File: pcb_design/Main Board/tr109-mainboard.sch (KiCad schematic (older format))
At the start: 23 parts, among them J1 Raspberry Pi Zero W, J2 ST7735_Screen, J3 Conn_01x04_Female, J4 Conn_01x09_Female, J5 Conn_01x03_Female, J6 Conn_01x02_Female-Connector, J7 Conn_01x03_Female, Q1 2N2222A, U1 CAP1208, U2 74HC595

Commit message: cleanup and revisions
changes to the sensor and main boards
clean up of the blender file to remove some deprecated meshes
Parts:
- removed C2: 10uF, Capacitor_SMD:C_0603_1608Metric_Pad1.05x0.95mm_HandSolder, symbol Device:CP
- removed Q1: 2N2222A, footprints:SSTA06HZGT116, symbol dk_Transistors-Bipolar-BJT-Single:2N2222A
- removed R3: 15k, Resistor_SMD:R_0603_1608Metric_Pad1.05x0.95mm_HandSolder, symbol Device:R
- removed R4: 8, Resistor_SMD:R_0603_1608Metric_Pad1.05x0.95mm_HandSolder, symbol Device:R
- added C2: 1uF, Capacitor_SMD:C_0603_1608Metric_Pad1.05x0.95mm_HandSolder, symbol Device:C
- added C3: 10uF, Capacitor_SMD:C_0603_1608Metric_Pad1.05x0.95mm_HandSolder, symbol Device:C
- added RV1: 10K, Potentiometer_SMD:Potentiometer_Bourns_3214W_Vertical, symbol Device:R_POT
- added U3: PAM8302AAS, Main Board:SOIC-8, symbol Amplifier_Audio:PAM8302AAS
- C1: value 100nF -> 1uF
- J6: symbol oshpark-2layer-rescue:Conn_01x02_Female-Connector -> Connector:Conn_01x02_Female
- R1: value 270 -> 100
- R2: value 150 -> 100
- U1: symbol Sensor_Touch:CAP1208 -> tr109-mainboard-rescue:CAP1208-Sensor_Touch
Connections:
- wire segments 24 -> 35
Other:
- moved on the sheet: J6
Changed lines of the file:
@@
 LED4
 $Comp
-L Sensor_Touch:CAP1208 U1
+L tr109-mainboard-rescue:CAP1208-Sensor_Touch U1
 U 1 1 5F245663
 P 4100 5800
@@
 Text GLabel 2450 1250 1    50   Input ~ 0
 5V
-Text GLabel 1750 2050 0    50   Input ~ 0
+Text GLabel 1750 2150 0    50   Input ~ 0
 Hall_Effect_Sensor
 Text GLabel 3500 5450 0    50   Input ~ 0
@@
 Hall_Effect_Sensor
 $Comp
-L dk_Transistors-Bipolar-BJT-Single:2N2222A Q1
-U 1 1 5FC250B2
-P 6400 1450
-F 0 "Q1" H 6588 1503 60  0000 L CNN
-F 1 "2N2222A" H 6588 1397 60  0000 L CNN
-F 2 "footprints:SSTA06HZGT116" H 6600 1650 60  0001 L CNN
-F 3 "https://my.centralsemi.com/get_document.php?cmp=1&mergetype=pd&mergepath=pd&pdf_id=2N2221A.PDF" H 6600 1750 60  0001 L CNN
-F 4 "2N2222ACS-ND" H 6600 1850 60  0001 L CNN "Digi-Key_PN"
-F 5 "2N2222A" H 6600 1950 60  0001 L CNN "MPN"
-F 6 "Discrete Semiconductor Products" H 6600 2050 60  0001 L CNN "Category"
-F 7 "Transistors - Bipolar (BJT) - Single" H 6600 2150 60  0001 L CNN "Family"
-F 8 "https://my.centralsemi.com/get_document.php?cmp=1&mergetype=pd&mergepath=pd&pdf_id=2N2221A.PDF" H 6600 2250 60  0001 L CNN "DK_Datasheet_Link"
-F 9 "/product-detail/en/central-semiconductor-corp/2N2222A/2N2222ACS-ND/4806845" H 6600 2350 60  0001 L CNN "DK_Detail_Page"
-F 10 "TRANS NPN 40V 0.8A TO-18" H 6600 2450 60  0001 L CNN "Description"
-F 11 "Central Semiconductor Corp" H 6600 2550 60  0001 L CNN "Manufacturer"
-F 12 "Active" H 6600 2650 60  0001 L CNN "Status"
-	1    6400 1450
-	1    0    0    -1
-$EndComp
-$Comp
-L Device:R R4
-U 1 1 5FC269BF
-P 6650 1100
-F 0 "R4" V 6443 1100 50  0000 C CNN
-F 1 "8" V 6534 1100 50  0000 C CNN
-F 2 "Resistor_SMD:R_0603_1608Metric_Pad1.05x0.95mm_HandSolder" V 6580 1100 50  0001 C CNN
-F 3 "~" H 6650 1100 50  0001 C CNN
-	1    6650 1100
-	0    1    1    0
-$EndComp
-$Comp
-L Device:R R3
-U 1 1 5FC2856A
-P 6200 1150
-F 0 "R3" H 6130 1104 50  0000 R CNN
-F 1 "15k" H 6130 1195 50  0000 R CNN
-F 2 "Resistor_SMD:R_0603_1608Metric_Pad1.05x0.95mm_HandSolder" V 6130 1150 50  0001 C CNN
-F 3 "~" H 6200 1150 50  0001 C CNN
-	1    6200 1150
-	-1   0    0    1
-$EndComp
-$Comp
-L oshpark-2layer-rescue:Conn_01x02_Female-Connector J6
+L Connector:Conn_01x02_Female J6
 U 1 1 5FC2A999
-P 7200 850
-F 0 "J6" H 7228 826 50  0000 L CNN
-F 1 "Conn_01x02_Female-Connector" H 7228 735 50  0000 L CNN
-F 2 "Connector_PinHeader_2.54mm:PinHeader_1x02_P2.54mm_Vertical" H 7200 850 50  0001 C CNN
-F 3 "" H 7200 850 50  0001 C CNN
-	1    7200 850
-	1    0    0    -1
-$EndComp
-Wire Wire Line
-	6500 1100 6500 1250
-Wire Wire Line
-	6800 1100 7000 1100
-Wire Wire Line
-	7000 1100 7000 950
-Wire Wire Line
-	7000 850  6200 850
-Wire Wire Line
-	6200 850  6200 1000
-Wire Wire Line
-	6200 1300 6200 1450
-$Comp
-L Device:C C1
-U 1 1 5FC2DDBE
-P 5800 1600
-F 0 "C1" H 5915 1646 50  0000 L CNN
-F 1 "100nF" H 5915 1555 50  0000 L CNN
-F 2 "Capacitor_SMD:C_0603_1608Metric_Pad1.05x0.95mm_HandSolder" H 5838 1450 50  0001 C CNN
-F 3 "~" H 5800 1600 50  0001 C CNN
-	1    5800 1600
-	1    0    0    -1
-$EndComp
-$Comp
-L Device:CP C2
-U 1 1 5FC2F329
-P 6000 1450
-F 0 "C2" V 6255 1450 50  0000 C CNN
-F 1 "10uF" V 6164 1450 50  0000 C CNN
-F 2 "Capacitor_SMD:C_0603_1608Metric_Pad1.05x0.95mm_HandSolder" H 6038 1300 50  0001 C CNN
-F 3 "~" H 6000 1450 50  0001 C CNN
-	1    6000 1450
-	0    -1   -1   0
-$EndComp
-Wire Wire Line
-	6200 1450 6150 1450
-Connection ~ 6200 1450
-Wire Wire Line
-	5850 1450 5800 1450
-Wire Wire Line
-	6500 1750 6500 1650
-$Comp
-L Device:R R2
-U 1 1 5FC313ED
-P 5450 1600
-F 0 "R2" H 5380 1554 50  0000 R CNN
-F 1 "150" H 5380 1645 50  0000 R CNN
-F 2 "Resistor_SMD:R_0603_1608Metric_Pad1.05x0.95mm_HandSolder" V 5380 1600 50  0001 C CNN
-F 3 "~" H 5450 1600 50  0001 C CNN
-	1    5450 1600
-	-1   0    0    1
-$EndComp
-Wire Wire Line
-	5800 1750 5450 1750
-Wire Wire Line
-	5800 1450 5450 1450
-Connection ~ 5800 1450
-$Comp
-L Device:R R1
-U 1 1 5FC32D30
-P 5200 1450
-F 0 "R1" V 5407 1450 50  0000 C CNN
-F 1 "270" V 5316 1450 50  0000 C CNN
-F 2 "Resistor_SMD:R_0603_1608Metric_Pad1.05x0.95mm_HandSolder" V 5130 1450 50  0001 C CNN
-F 3 "~" H 5200 1450 50  0001 C CNN
-	1    5200 1450
-	0    -1   -1   0
-$EndComp
-Wire Wire Line
-	5450 1450 5350 1450
-Connection ~ 5450 1450
+P 6700 1500
+F 0 "J6" H 6728 1476 50  0000 L CNN
+F 1 "Conn_01x02_Female-Connector" H 6728 1385 50  0000 L CNN
+F 2 "Connector_PinHeader_2.54mm:PinHeader_1x02_P2.54mm_Vertical" H 6700 1500 50  0001 C CNN
+F 3 "" H 6700 1500 50  0001 C CNN
+	1    6700 1500
+	1    0    0    -1
+$EndComp
 Text GLabel 3350 3350 2    50   Input ~ 0
 AUDIO
-Text GLabel 5050 1450 0    50   Input ~ 0
-AUDIO
-Text GLabel 6200 850  1    50   Input ~ 0
-5V
-Text GLabel 5450 1750 3    50   Input ~ 0
-GND
-Text GLabel 4700 1900 0    50   Input ~ 0
-Bat_GPIO
 Text GLabel 3350 2350 2    50   Input ~ 0
 Bat_GPIO
@@
 Text GLabel 1750 3150 0    50   Input ~ 0
 Hall_Effect_Sensor2
-Text GLabel 6500 1750 3    50   Input ~ 0
-GND
 Text GLabel 3500 6050 0    50   Input ~ 0
 Cap_7
 Text GLabel 4700 6050 2    50   Input ~ 0
 Cap_7
+$Comp
+L Amplifier_Audio:PAM8302AAS U3
+U 1 1 60ABCA11
+P 5850 1700
+F 0 "U3" H 6100 2600 50  0000 C CNN
+F 1 "PAM8302AAS" H 6100 2500 50  0000 C CNN
+F 2 "Main Board:SOIC-8" H 5850 1700 50  0001 C CNN
+F 3 "https://www.diodes.com/assets/Datasheets/PAM8302A.pdf" H 5850 1700 50  0001 C CNN
+	1    5850 1700
+	1    0    0    -1
+$EndComp
+$Comp
+L Device:R_POT RV1
+U 1 1 60ABDB90
+P 4700 1200
+F 0 "RV1" H 4631 1246 50  0000 R CNN
+F 1 "10K" H 4631 1155 50  0000 R CNN
+F 2 "Potentiometer_SMD:Potentiometer_Bourns_3214W_Vertical" H 4700 1200 50  0001 C CNN
+F 3 "~" H 4700 1200 50  0001 C CNN
+	1    4700 1200
+	1    0    0    -1
+$EndComp
+$Comp
+L Device:C C1
+U 1 1 60ABF3BD
+P 5000 1200
+F 0 "C1" V 4748 1200 50  0000 C CNN
+F 1 "1uF" V 4839 1200 50  0000 C CNN
+F 2 "Capacitor_SMD:C_0603_1608Metric_Pad1.05x0.95mm_HandSolder" H 5038 1050 50  0001 C CNN
+F 3 "~" H 5000 1200 50  0001 C CNN
+	1    5000 1200
+	0    1    1    0
+$EndComp
+$Comp
+L Device:R R1
+U 1 1 60ABFD3B
+P 5300 1200
+F 0 "R1" V 5093 1200 50  0000 C CNN
+F 1 "100" V 5184 1200 50  0000 C CNN
+F 2 "Resistor_SMD:R_0603_1608Metric_Pad1.05x0.95mm_HandSolder" V 5230 1200 50  0001 C CNN
+F 3 "~" H 5300 1200 50  0001 C CNN
+	1    5300 1200
+	0    1    1    0
+$EndComp
+$Comp
+L Device:R R2
+U 1 1 60AC08CB
+P 5300 1700
+F 0 "R2" V 5093 1700 50  0000 C CNN
+F 1 "100" V 5184 1700 50  0000 C CNN
+F 2 "Resistor_SMD:R_0603_1608Metric_Pad1.05x0.95mm_HandSolder" V 5230 1700 50  0001 C CNN
+F 3 "~" H 5300 1700 50  0001 C CNN
+	1    5300 1700
+	0    1    1    0
+$EndComp
+$Comp
+L Device:C C2
+U 1 1 60AC1063
+P 5000 1700
+F 0 "C2" V 4748 1700 50  0000 C CNN
+F 1 "1uF" V 4839 1700 50  0000 C CNN
+F 2 "Capacitor_SMD:C_0603_1608Metric_Pad1.05x0.95mm_HandSolder" H 5038 1550 50  0001 C CNN
+F 3 "~" H 5000 1700 50  0001 C CNN
+	1    5000 1700
+	0    1    1    0
+$EndComp
+Wire Wire Line
+	5450 1200 5450 1500
+Text GLabel 4850 2000 3    50   Input ~ 0
+GND
+Wire Wire Line
+	4700 1350 4850 1350
+Wire Wire Line
+	4850 1350 4850 1700
+Wire Wire Line
+	4850 1700 4850 2000
+Connection ~ 4850 1700
+Text GLabel 4250 900  0    50   Input ~ 0
+AUDIO
+Text GLabel 5150 2050 0    50   Input ~ 0
+5V
+Text GLabel 5250 2350 3    50   Input ~ 0
+GND
+Text GLabel 5850 2100 3    50   Input ~ 0
+GND
+$Comp
+L Device:C C3
+U 1 1 60AC6DC2
+P 5250 2200
+F 0 "C3" H 5135 2154 50  0000 R CNN
+F 1 "10uF" H 5135 2245 50  0000 R CNN
+F 2 "Capacitor_SMD:C_0603_1608Metric_Pad1.05x0.95mm_HandSolder" H 5288 2050 50  0001 C CNN
+F 3 "~" H 5250 2200 50  0001 C CNN
+	1    5250 2200
+	-1   0    0    1
+$EndComp
+Connection ~ 5250 2050
+Wire Wire Line
+	5250 2050 5150 2050
+Wire Wire Line
+	5850 1350 5850 1300
+Wire Wire Line
+	5850 1150 6350 1150
+Wire Wire Line
+	6350 1150 6350 2450
+Wire Wire Line
+	6350 2450 5600 2450
+Wire Wire Line
+	5600 2450 5600 2050
+Connection ~ 5850 1300
+Wire Wire Line
+	5850 1300 5850 1150
+Wire Wire Line
+	5250 2050 5450 2050
+Wire Wire Line
+	5450 1900 5450 2050
+Connection ~ 5450 2050
+Wire Wire Line
+	5450 2050 5600 2050
+Wire Wire Line
+	6250 1500 6500 1500
+Wire Wire Line
+	6250 1700 6500 1700
+Wire Wire Line
+	6500 1700 6500 1600
+Wire Wire Line
+	4250 900  4700 900
+Wire Wire Line
+	4700 900  4700 1050
+Wire Wire Line
+	4150 5750 4150 5800
+Wire Wire Line
+	4000 5800 4050 5800
+Wire Wire Line
+	4050 5800 4050 5750
+Wire Wire Line
+	6750 1400 6750 1350
+Entry Wire Line
+	9350 6400 9450 6500
 $EndSCHEMATC

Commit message: Pcb and shell design work
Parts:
- J4: value Conn_01x09_Female -> Conn_01x11_Female; footprint Connector_PinHeader_2.54mm:PinHeader_1x09_P2.54mm_Vertical -> Connector_PinHeader_2.54mm:PinHeader_1x11_P2.54mm_Vertical; symbol Connector:Conn_01x09_Female -> Connector:Conn_01x11_Female
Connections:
- net labels added: Cap_8, Shift_Clock_Sensor_Board, Shift_Latch_Sensor_Board, Shift_Serial_Sensor_Board
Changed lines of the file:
@@
 Text GLabel 2450 1250 1    50   Input ~ 0
 5V
-Text GLabel 1750 2150 0    50   Input ~ 0
+Text GLabel 3350 3250 2    50   Input ~ 0
 Hall_Effect_Sensor
 Text GLabel 3500 5450 0    50   Input ~ 0
@@
 Text GLabel 8400 2650 0    50   Input ~ 0
 LED5
-Text GLabel 9200 4000 0    50   Input ~ 0
+Text GLabel 9200 3900 0    50   Input ~ 0
 Cap_6
-Text GLabel 9200 3900 0    50   Input ~ 0
+Text GLabel 9200 3800 0    50   Input ~ 0
 Cap_5
-Text GLabel 9200 3800 0    50   Input ~ 0
+Text GLabel 9200 3700 0    50   Input ~ 0
 Cap_4
-Text GLabel 9200 3700 0    50   Input ~ 0
+Text GLabel 9200 3600 0    50   Input ~ 0
 Cap_3
-Text GLabel 9200 3600 0    50   Input ~ 0
+Text GLabel 9200 3500 0    50   Input ~ 0
 Cap_2
-Text GLabel 9200 3500 0    50   Input ~ 0
+Text GLabel 9200 3400 0    50   Input ~ 0
 Cap_1
-Text GLabel 9200 3400 0    50   Input ~ 0
+Text GLabel 9200 3300 0    50   Input ~ 0
 Bat_GPIO
+Text GLabel 9200 3100 0    50   Input ~ 0
+GND
 Text GLabel 9200 3200 0    50   Input ~ 0
-GND
-Text GLabel 9200 3300 0    50   Input ~ 0
 5V
 $Comp
@@
 GND
 $Comp
-L Connector:Conn_01x09_Female J4
+L Connector:Conn_01x11_Female J4
 U 1 1 5F576896
 P 9400 3600
 F 0 "J4" H 9428 3626 50  0000 L CNN
-F 1 "Conn_01x09_Female" H 9428 3535 50  0000 L CNN
-F 2 "Connector_PinHeader_2.54mm:PinHeader_1x09_P2.54mm_Vertical" H 9400 3600 50  0001 C CNN
+F 1 "Conn_01x11_Female" H 9428 3535 50  0000 L CNN
+F 2 "Connector_PinHeader_2.54mm:PinHeader_1x11_P2.54mm_Vertical" H 9400 3600 50  0001 C CNN
 F 3 "~" H 9400 3600 50  0001 C CNN
 	1    9400 3600
@@
 Text GLabel 9250 1450 0    50   Input ~ 0
 Hall_Effect_Sensor2
-Text GLabel 1750 3150 0    50   Input ~ 0
+Text GLabel 3350 2250 2    50   Input ~ 0
 Hall_Effect_Sensor2
 Text GLabel 3500 6050 0    50   Input ~ 0
 Cap_7
 Text GLabel 4700 6050 2    50   Input ~ 0
-Cap_7
+Cap_8
 $Comp
 L Amplifier_Audio:PAM8302AAS U3
@@
 Wire Wire Line
 	6750 1400 6750 1350
-Entry Wire Line
-	9350 6400 9450 6500
+Text GLabel 1750 2350 0    50   Input ~ 0
+Shift_Serial_Sensor_Board
+Text GLabel 1750 2550 0    50   Input ~ 0
+Shift_Latch_Sensor_Board
+Text GLabel 1750 3150 0    50   Input ~ 0
+Shift_Clock_Sensor_Board
+Text GLabel 9200 4000 0    50   Input ~ 0
+Cap_7
+Text GLabel 9200 4100 0    50   Input ~ 0
+Cap_8
 $EndSCHEMATC

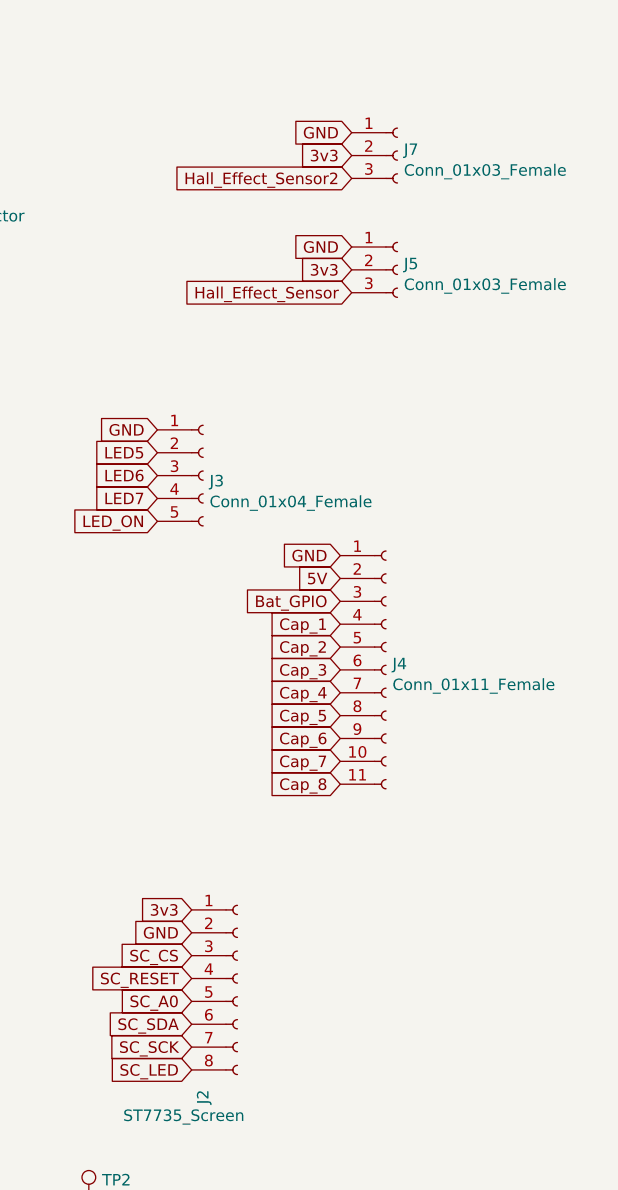
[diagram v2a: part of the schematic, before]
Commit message: Rev 3 board changes, blender file changes
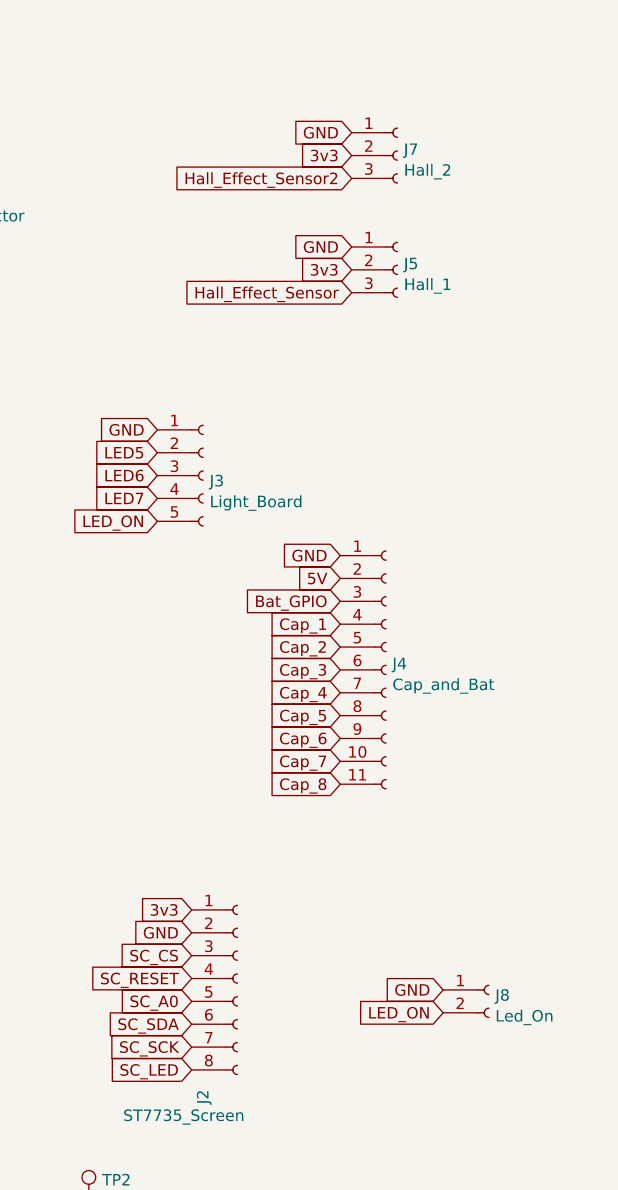
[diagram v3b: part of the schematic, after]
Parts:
- added J8: Led_On, Connector_PinHeader_2.54mm:PinHeader_1x02_P2.54mm_Vertical, symbol Connector:Conn_01x02_Female
- J3: value Conn_01x04_Female -> Light_Board
- J4: value Conn_01x11_Female -> Cap_and_Bat
- J5: value Conn_01x03_Female -> Hall_1
- J7: value Conn_01x03_Female -> Hall_2
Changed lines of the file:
@@
 P 8600 2750
 F 0 "J3" H 8628 2726 50  0000 L CNN
-F 1 "Conn_01x04_Female" H 8628 2635 50  0000 L CNN
+F 1 "Light_Board" H 8628 2635 50  0000 L CNN
 F 2 "Connector_PinHeader_2.54mm:PinHeader_1x05_P2.54mm_Vertical" H 8600 2750 50  0001 C CNN
 F 3 "~" H 8600 2750 50  0001 C CNN
@@
 P 9400 3600
 F 0 "J4" H 9428 3626 50  0000 L CNN
-F 1 "Conn_01x11_Female" H 9428 3535 50  0000 L CNN
+F 1 "Cap_and_Bat" H 9428 3535 50  0000 L CNN
 F 2 "Connector_PinHeader_2.54mm:PinHeader_1x11_P2.54mm_Vertical" H 9400 3600 50  0001 C CNN
 F 3 "~" H 9400 3600 50  0001 C CNN
@@
 P 9450 1850
 F 0 "J5" H 9478 1876 50  0000 L CNN
-F 1 "Conn_01x03_Female" H 9478 1785 50  0000 L CNN
+F 1 "Hall_1" H 9478 1785 50  0000 L CNN
 F 2 "Connector_PinHeader_2.54mm:PinHeader_1x03_P2.54mm_Vertical" H 9450 1850 50  0001 C CNN
 F 3 "~" H 9450 1850 50  0001 C CNN
@@
 P 9450 1350
 F 0 "J7" H 9478 1376 50  0000 L CNN
-F 1 "Conn_01x03_Female" H 9478 1285 50  0000 L CNN
+F 1 "Hall_2" H 9478 1285 50  0000 L CNN
 F 2 "Connector_PinHeader_2.54mm:PinHeader_1x03_P2.54mm_Vertical" H 9450 1350 50  0001 C CNN
 F 3 "~" H 9450 1350 50  0001 C CNN
@@
 Text GLabel 9200 4100 0    50   Input ~ 0
 Cap_8
+$Comp
+L Connector:Conn_01x02_Female J8
+U 1 1 60C056D7
+P 9850 5000
+F 0 "J8" H 9878 4976 50  0000 L CNN
+F 1 "Led_On" H 9878 4885 50  0000 L CNN
+F 2 "Connector_PinHeader_2.54mm:PinHeader_1x02_P2.54mm_Vertical" H 9850 5000 50  0001 C CNN
+F 3 "~" H 9850 5000 50  0001 C CNN
+	1    9850 5000
+	1    0    0    -1
+$EndComp
+Text GLabel 9650 5100 0    50   Input ~ 0
+LED_ON
+Text GLabel 9650 5000 0    50   Input ~ 0
+GND
 $EndSCHEMATC

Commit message: Pcb and enclosure changes for proto 01
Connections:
- net labels added: BUT1, BUT2, BUT3
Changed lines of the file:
@@
 Text GLabel 9650 5000 0    50   Input ~ 0
 GND
+Text GLabel 1750 2050 0    50   Input ~ 0
+BUT1
+Text GLabel 1750 3250 0    50   Input ~ 0
+BUT2
+Text GLabel 1750 2750 0    50   Input ~ 0
+BUT3
 $EndSCHEMATC

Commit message: changes to shell and pcb
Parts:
- added J10: raw_audio_out, Connector_PinHeader_2.54mm:PinHeader_1x01_P2.54mm_Vertical, symbol Connector:Conn_01x01_Female
- added J9: i2c_bus, Connector_PinHeader_2.54mm:PinHeader_1x02_P2.54mm_Vertical, symbol Connector:Conn_01x02_Female
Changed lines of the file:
@@
 Text GLabel 1750 2750 0    50   Input ~ 0
 BUT3
+$Comp
+L Connector:Conn_01x02_Female J9
+U 1 1 610ACCCB
+P 9850 5600
+F 0 "J9" H 9878 5576 50  0000 L CNN
+F 1 "i2c_bus" H 9878 5485 50  0000 L CNN
+F 2 "Connector_PinHeader_2.54mm:PinHeader_1x02_P2.54mm_Vertical" H 9850 5600 50  0001 C CNN
+F 3 "~" H 9850 5600 50  0001 C CNN
+	1    9850 5600
+	1    0    0    -1
+$EndComp
+Text GLabel 9650 5700 0    50   Input ~ 0
+SDA
+Text GLabel 9650 5600 0    50   Input ~ 0
+SCL
+$Comp
+L Connector:Conn_01x01_Female J10
+U 1 1 610B2E38
+P 9850 6000
+F 0 "J10" H 9878 6026 50  0000 L CNN
+F 1 "raw_audio_out" H 9878 5935 50  0000 L CNN
+F 2 "Connector_PinHeader_2.54mm:PinHeader_1x01_P2.54mm_Vertical" H 9850 6000 50  0001 C CNN
+F 3 "~" H 9850 6000 50  0001 C CNN
+	1    9850 6000
+	1    0    0    -1
+$EndComp
+Text GLabel 9650 6000 0    50   Input ~ 0
+AUDIO
 $EndSCHEMATC
